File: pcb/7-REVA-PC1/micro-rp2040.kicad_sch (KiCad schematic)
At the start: 58 parts, among them J201 Conn_01x03, J202 TYPE-C-31-M-12, Q1 2N7002KT, Q5 2N7002KT, SW101 TS3425BA 098 2.5H 250gf, SW102 TS3315A 250gf 025, U1 RP2350B, U102 W25Q128JVSIQ, U105 MT29F1G01ABAFDWB, U16 SP3002-04JTG, U3 TLV74311PDBVR, U401 ME6211A33PG-N, U8 APS6404L-3SQR-ZR, Y101 ABM8-272-T3

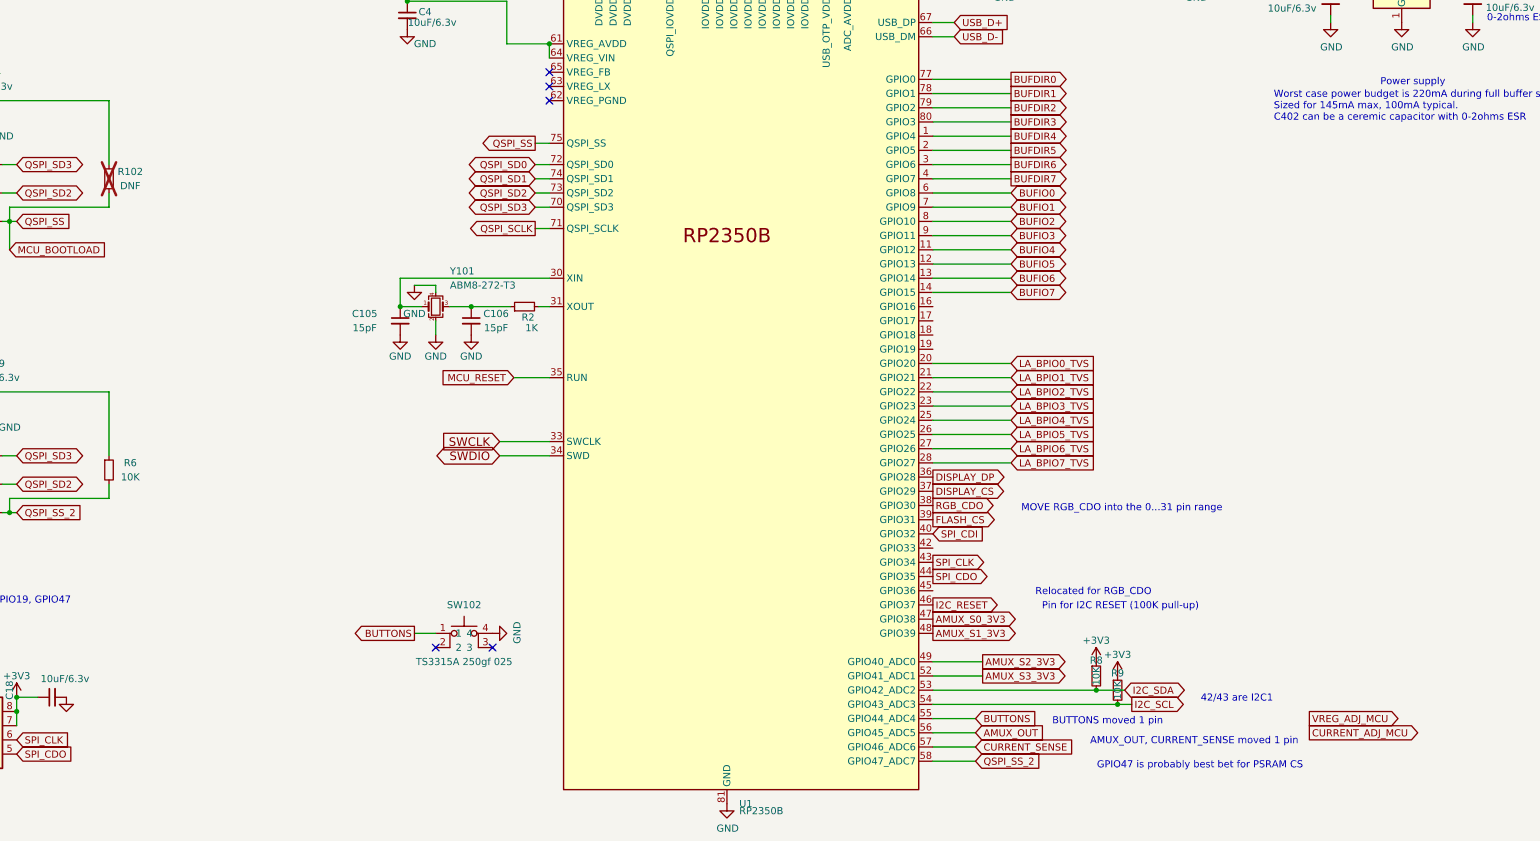
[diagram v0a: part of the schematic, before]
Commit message: Remove DNF footprints, locate PWM pins for power supply adjustment. Change PWM op-amp to DFN and buffer also the CURRENT_ADJ. Remove a FET gate resistor from current limiter.
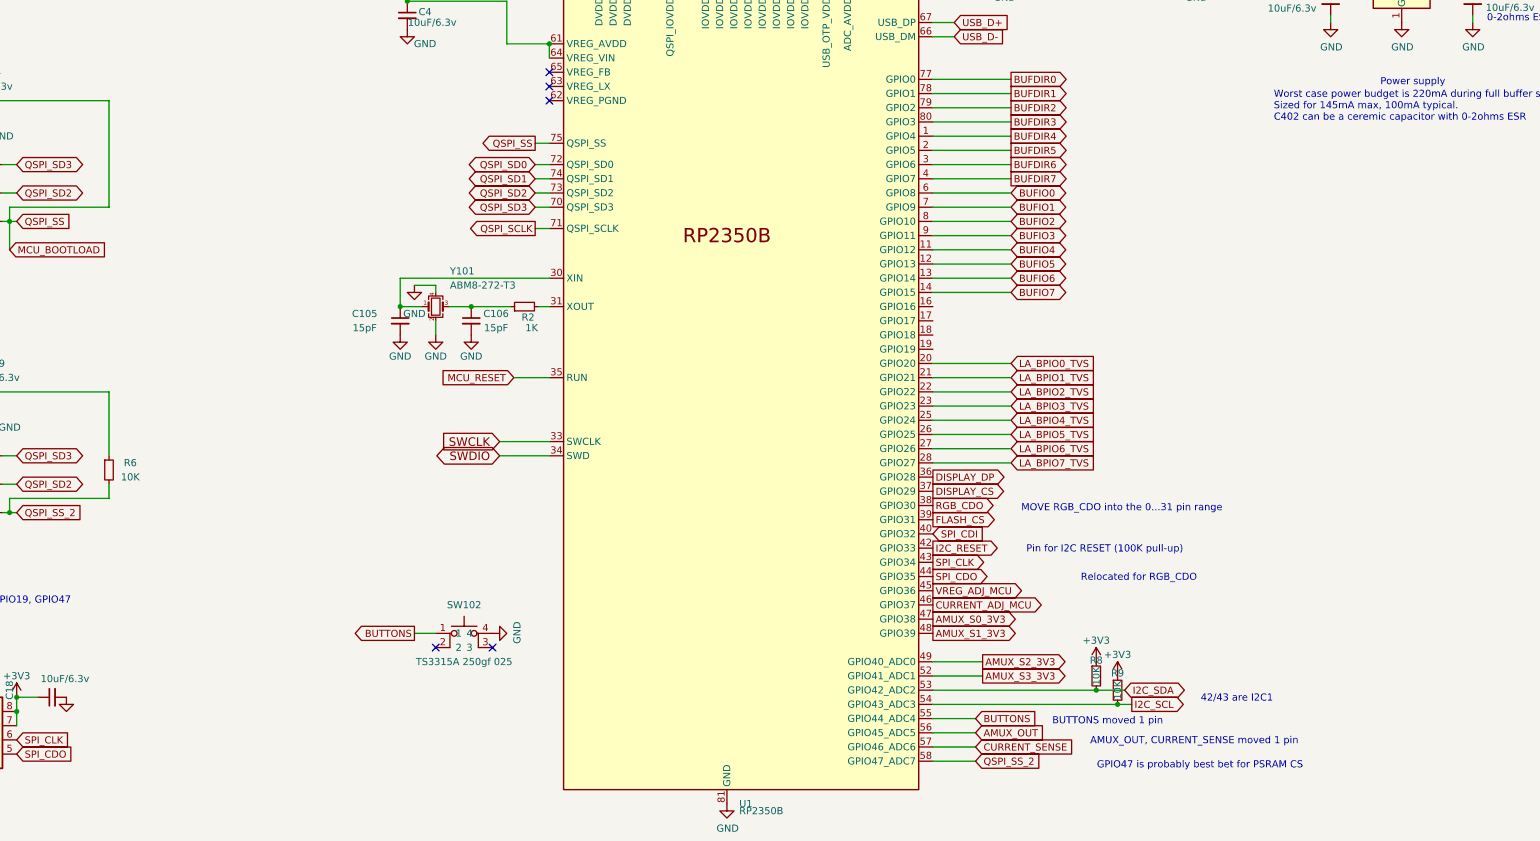
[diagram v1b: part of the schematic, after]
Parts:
- removed R102: DNF, Resistor_SMD:R_0402_1005Metric, symbol Device:R_Small
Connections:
- net MCU_BOOTLOAD is gone; now on net +3V3: R12.2, U1.75 (QSPI_SS), U102.1 (CS)
- net CURRENT_ADJ_MCU: now also U1.46 (GPIO37)
- net I2C_RESET: now also U1.42 (GPIO33); no longer U1.46 (GPIO37)
- net VREG_ADJ_MCU: now also U1.45 (GPIO36)
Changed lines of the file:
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@@
 	(wire
 		(pts
-			(xy 149.86 104.14) (xy 149.86 101.6)
+			(xy 149.86 85.09) (xy 149.86 104.14)
 		)
 		(stroke
@@
 	(wire
 		(pts
-			(xy 149.86 96.52) (xy 149.86 85.09)
-		)
-		(stroke
-			(width 0)
-			(type default)
-		)
-	)
-	(wire
-		(pts
 			(xy 353.06 41.91) (xy 353.06 46.99)
 		)
@@
 	(text "Pin for I2C RESET (100K pull-up)\n"
 		(exclude_from_sim no)
-		(at 330.708 175.514 0)
+		(at 327.914 165.354 0)
 		(effects
 			(font
@@
 	(text "Relocated for RGB_CDO"
 		(exclude_from_sim no)
-		(at 325.882 172.974 0)
+		(at 334.01 170.434 0)
 		(effects
 			(font
@@
 	(global_label "VREG_ADJ_MCU"
 		(shape output)
-		(at 364.49 195.58 0)
+		(at 297.18 172.72 0)
 		(effects
 			(font
@@
 		)
 		(property "Intersheetrefs" "${INTERSHEET_REFS}"
-			(at 364.49 195.58 0)
+			(at 297.18 172.72 0)
 			(effects
 				(font
@@
 	(global_label "CURRENT_ADJ_MCU"
 		(shape output)
-		(at 364.49 198.12 0)
+		(at 297.18 175.26 0)
 		(effects
 			(font
@@
 		)
 		(property "Intersheetrefs" "${INTERSHEET_REFS}"
-			(at 364.49 198.12 0)
+			(at 297.18 175.26 0)
 			(effects
 				(font
@@
 	(global_label "I2C_RESET"
 		(shape output)
-		(at 297.18 175.26 0)
+		(at 297.18 165.1 0)
 		(fields_autoplaced yes)
 		(effects
@@
 		)
 		(property "Intersheetrefs" "${INTERSHEET_REFS}"
-			(at 309.308 175.26 0)
+			(at 309.308 165.1 0)
 			(effects
 				(font
@@
 					(unit 1)
 				)
-			)
-		)
-	)
-	(symbol
-		(lib_id "Device:R_Small")
-		(at 149.86 99.06 0)
-		(unit 1)
-		(exclude_from_sim no)
-		(in_bom no)
-		(on_board yes)
-		(dnp yes)
-		(property "Reference" "R102"
-			(at 153.67 97.79 0)
-			(effects
-				(font
-					(size 1.27 1.27)
-				)
-			)
-		)
-		(property "Value" "DNF"
-			(at 153.67 100.33 0)
-			(effects
-				(font
-					(size 1.27 1.27)
-				)
-			)
-		)
-		(property "Footprint" "Resistor_SMD:R_0402_1005Metric"
-			(at 149.86 99.06 0)
-			(effects
-				(font
-					(size 1.27 1.27)
-				)
-				(hide yes)
-			)
-		)
-		(property "Datasheet" "~"
-			(at 149.86 99.06 0)
-			(effects
-				(font
-					(size 1.27 1.27)
-				)
-				(hide yes)
-			)
-		)
-		(property "Description" ""
-			(at 149.86 99.06 0)
-			(effects
-				(font
-					(size 1.27 1.27)
-				)
-				(hide yes)
-			)
-		)
-		(property "RMB" "0.006373"
-			(at 149.86 99.06 0)
-			(effects
-				(font
-					(size 1.27 1.27)
-				)
-				(hide yes)
-			)
-		)
-		(property "Supplier" "https://item.szlcsc.com/116008.html"
-			(at 149.86 99.06 0)
-			(effects
-				(font
-					(size 1.27 1.27)
-				)
-				(hide yes)
-			)
-		)
-		(property "Description_1" ""
-			(at 149.86 99.06 0)
-			(effects
-				(font
-					(size 1.27 1.27)
-				)
-				(hide yes)
-			)
-		)
-		(property "MAXIMUM_PACKAGE_HEIGHT" ""
-			(at 149.86 99.06 0)
-			(effects
-				(font
-					(size 1.27 1.27)
-				)
-				(hide yes)
-			)
-		)
-		(property "PARTREV" ""
-			(at 149.86 99.06 0)
-			(effects
-				(font
-					(size 1.27 1.27)
-				)
-				(hide yes)
-			)
-		)
-		(property "STANDARD" ""
-			(at 149.86 99.06 0)
-			(effects
-				(font
-					(size 1.27 1.27)
-				)
-				(hide yes)
-			)
-		)
-		(pin "1"
-		)
-		(pin "2"
-		)
-		(instances
-			(project "REV0"
-				(path "/1f56410a-eaac-4444-b0f7-cfd3531e22ac/00000000-0000-0000-0000-000060c8ec36"
-					(reference "R102")
-					(unit 1)
-				)

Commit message: cleanup microcontroller schematic
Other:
- note added: "1.1volt core voltage regulator"
- note added: "Bootloader or reset button"
- moved on the sheet: C1, C10, C104, C105, C106, C109, C11, C110, C111, C112, C113, C114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

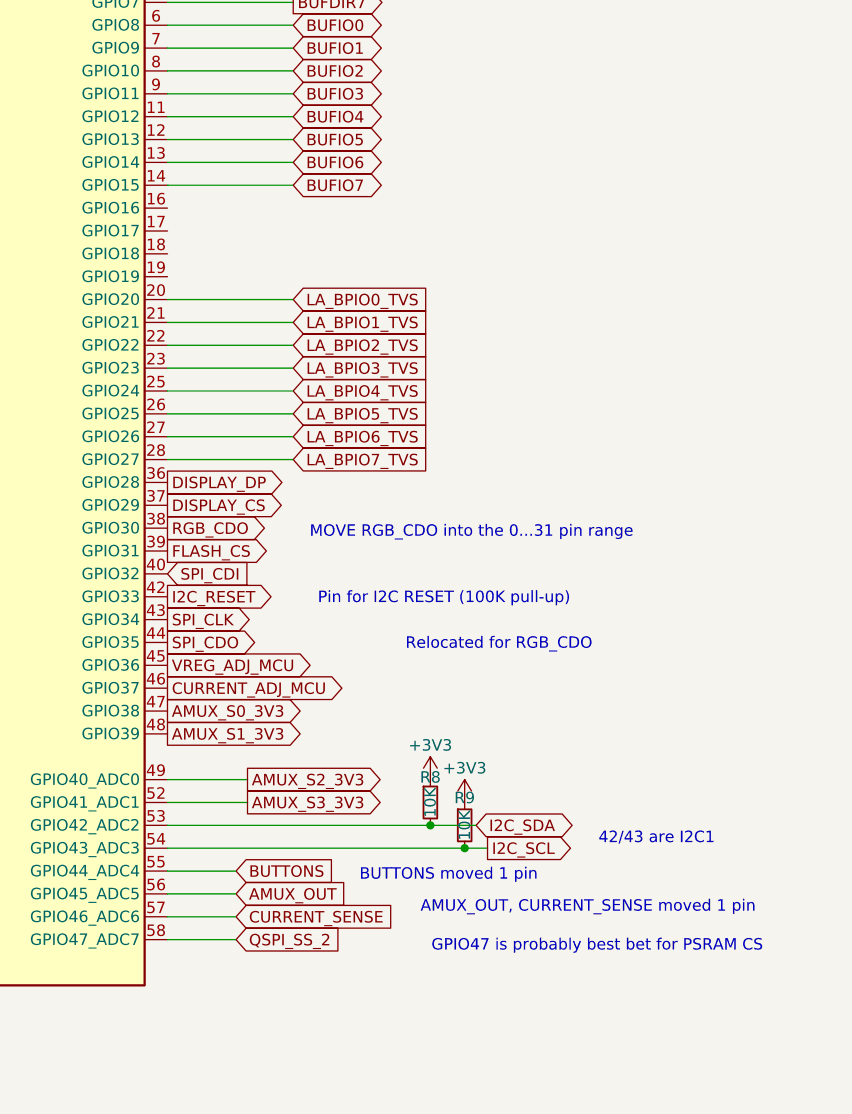
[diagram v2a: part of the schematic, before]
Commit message: Final I2C and PWM pin selection.
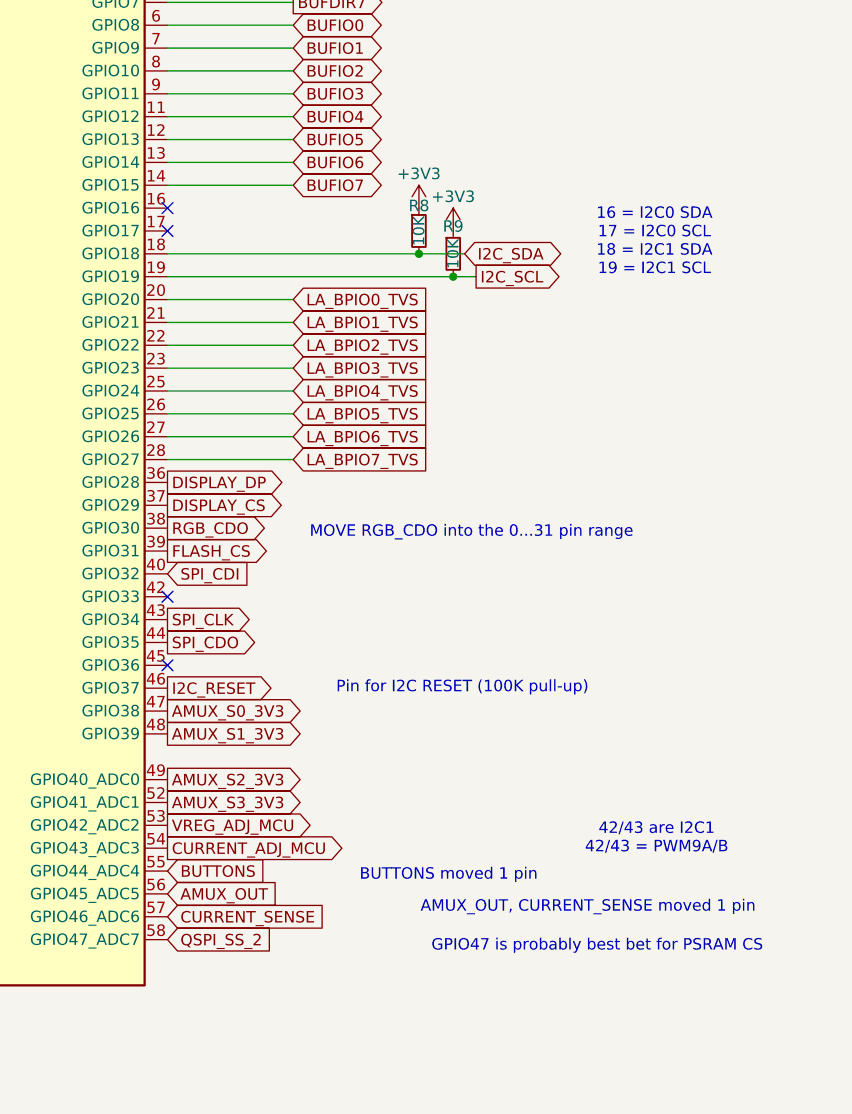
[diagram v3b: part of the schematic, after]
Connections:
- net CURRENT_ADJ_MCU: now also U1.54 (GPIO43_ADC3); no longer U1.46 (GPIO37)
- net I2C_RESET: now also U1.46 (GPIO37); no longer U1.42 (GPIO33)
- net I2C_SCL: now also U1.19 (GPIO19); no longer U1.54 (GPIO43_ADC3)
- net I2C_SDA: now also U1.18 (GPIO18); no longer U1.53 (GPIO42_ADC2)
- net VREG_ADJ_MCU: now also U1.53 (GPIO42_ADC2); no longer U1.45 (GPIO36)
- no-connect marks 9 -> 13
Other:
- note added: "16 = I2C0 SDA 17 = I2C0 SCL 18 = I2C1 SDA 19 = I2C1 SCL"
- note added: "42/43 are I2C1 42/43 = PWM9A/B"
- note removed: "42/43 are I2C1"
- note removed: "Relocated for RGB_CDO"
- moved on the sheet: R8, R9

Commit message: 7R1 PCB routed
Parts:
- Q1, Q5: footprint Package_TO_SOT_SMD:SOT-523 -> library:SOT-523
- U8: footprint Package_SON:Winbond_USON-8-1EP_3x2mm_P0.5mm_EP0.2x1.6mm -> library:USON-8-3x2mm_P0.5mm_EPthin
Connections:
- net +3V3: no longer R12.2, U1.75 (QSPI_SS), U102.1 (CS)
- net XL9555_~{INT}: now reaches U1.16 (GPIO16)
- new net MCU_BOOTLOAD: R12.2, U1.75 (QSPI_SS), U102.1 (CS)
- no-connect marks 13 -> 12
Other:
- moved on the sheet: R8, R9
